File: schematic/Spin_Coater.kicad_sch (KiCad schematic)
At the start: 97 parts, among them J1 USB_C_Receptacle_USB2.0_14P, J2 Motor Encoder In, J3 USB_B_Micro, M1 Hobbywing QuicRun 3650, M1A1 TestPoint, M1B1 TestPoint, M1C1 TestPoint, Q1 AONR21357, Q2 GSFN6982, Q3 GSFN6982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

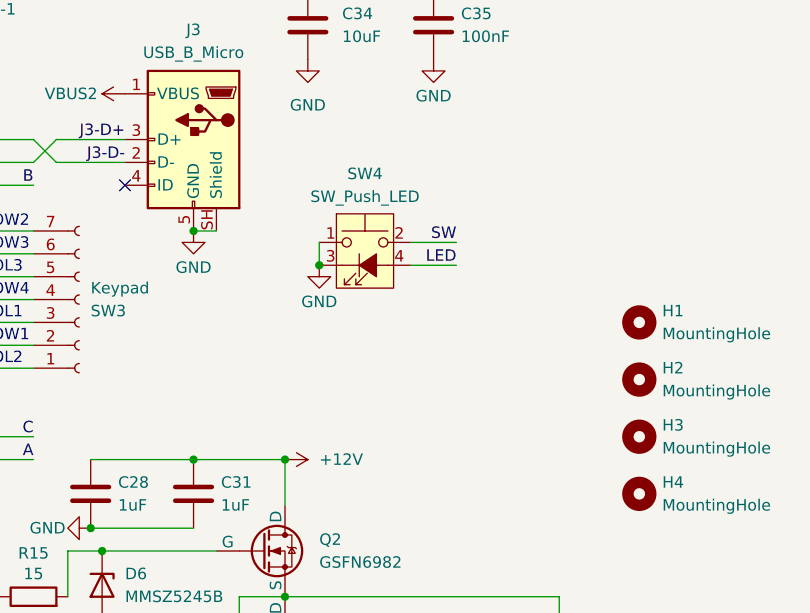
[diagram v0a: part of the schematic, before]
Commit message: Added button debouncing
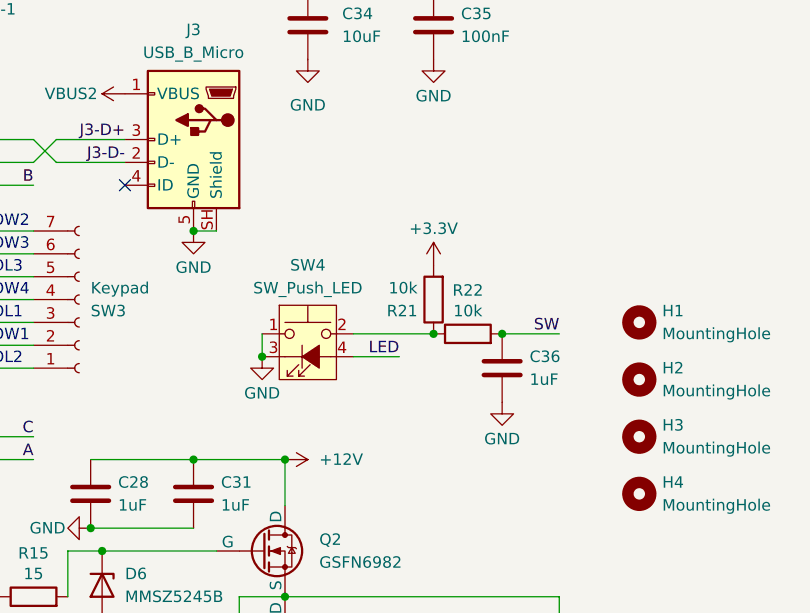
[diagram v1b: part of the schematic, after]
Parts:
- added C36: 1uF, Capacitor_SMD:C_0805_2012Metric, symbol Device:C
- added R21, R22: 10k, Resistor_SMD:R_0805_2012Metric, symbol Device:R
- M1A1, M1B1, M1C1: footprint footprints:TestPoint_THTPad_D5.0mm_Drill3.0mm -> footprints:TestPoint_THTPad_D5.5mm_Drill3.5mm
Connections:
- net +3.3V: now also R21.2
- net GND: now also C36.2
- net SW: now also C36.1, R22.2; no longer SW4.2
- new net: R21.1, R22.1, SW4.2
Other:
- moved on the sheet: SW4

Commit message: Hopefully final revision
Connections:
- net GND: no longer U2.9 (ISET)
- no-connect marks 17 -> 18
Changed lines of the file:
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@@
 	)
 	(no_connect
+		(at 71.12 59.69)
+	)
+	(no_connect
 		(at 74.93 185.42)
 	)
@@
 					(unit 1)
 				)
-			)
-		)
-	)
-	(symbol
-		(lib_id "power:GND")
-		(at 71.12 59.69 0)
-		(unit 1)
-		(body_style 1)
-		(exclude_from_sim no)
-		(in_bom yes)
-		(on_board yes)
-		(in_pos_files yes)
-		(dnp no)
-		(property "Reference" "#PWR019"
-			(at 71.12 66.04 0)
-			(hide yes)
-			(show_name no)
-			(do_not_autoplace no)
-			(effects
-				(font
-					(size 1.27 1.27)
-				)
-			)
-		)
-		(property "Value" "GND"
-			(at 71.12 63.754 0)
-			(show_name no)
-			(do_not_autoplace no)
-			(effects
-				(font
-					(size 1.27 1.27)
-				)
-			)
-		)
-		(property "Footprint" ""
-			(at 71.12 59.69 0)
-			(hide yes)
-			(show_name no)
-			(do_not_autoplace no)
-			(effects
-				(font
-					(size 1.27 1.27)
-				)
-			)
-		)
-		(property "Datasheet" ""
-			(at 71.12 59.69 0)
-			(hide yes)
-			(show_name no)
-			(do_not_autoplace no)
-			(effects
-				(font
-					(size 1.27 1.27)
-				)
-			)
-		)
-		(property "Description" "Power symbol creates a global label with name \"GND\" , ground"
-			(at 71.12 59.69 0)
-			(hide yes)
-			(show_name no)
-			(do_not_autoplace no)
-			(effects
-				(font
-					(size 1.27 1.27)
-				)
-			)
-		)
-		(pin "1"
-		)
-		(instances
-			(project "Spin_Coater"
-				(path "/2a6934bd-4ba7-41c7-a1b4-d8fafbfb083c"
-					(reference "#PWR019")
-					(unit 1)
-				)
